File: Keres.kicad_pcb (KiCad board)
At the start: 6 copper layers, 110 x 70 mm, 168 parts, among them J1 XT90M, J2 DSUB44S_HD, J3 U_FL-R-SMT-1_10_, J4 2.54mm Pin Header, Q1 SiS443DN, Q2 SQJQ116EL, Q3 SQJQ116EL, Q4 SQJQ116EL, Q5 SQJQ116EL, U1 TLV76133DCY, U10 LT6106, U11 LT6106, U12 LT6106, U13 MAX11616, U14 LT6106, U15 LT6106, U16 LT6106, U17 LT6106, U18 MAX11614, U19 LT6106, U2 LM22678TJ-5, U3 LM22678TJ-5, U4 LM22678TJ-5, U5 BMP280, U6 MAX-M10S, U7 Teensy 4.0, U8 MPU-6050, U9 LT6106

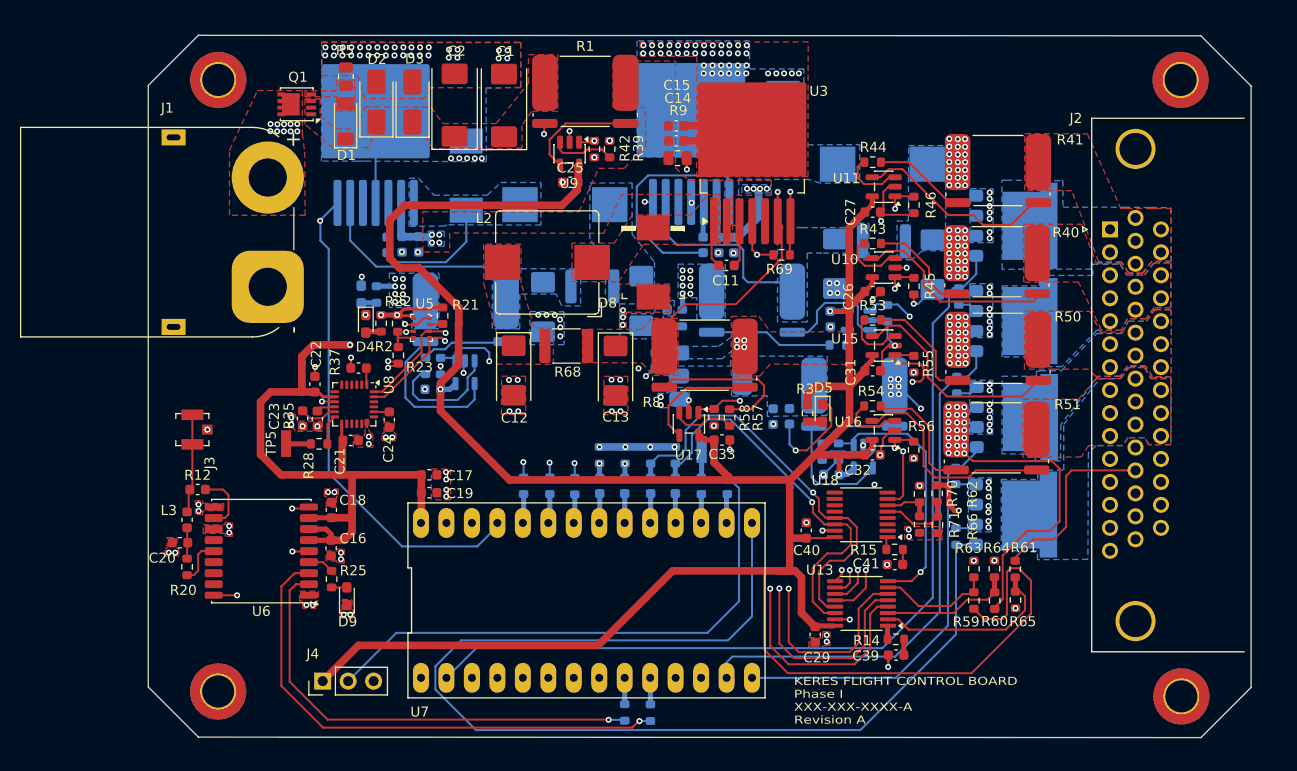
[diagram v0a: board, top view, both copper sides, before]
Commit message: Fix DRC Errors and Warnings
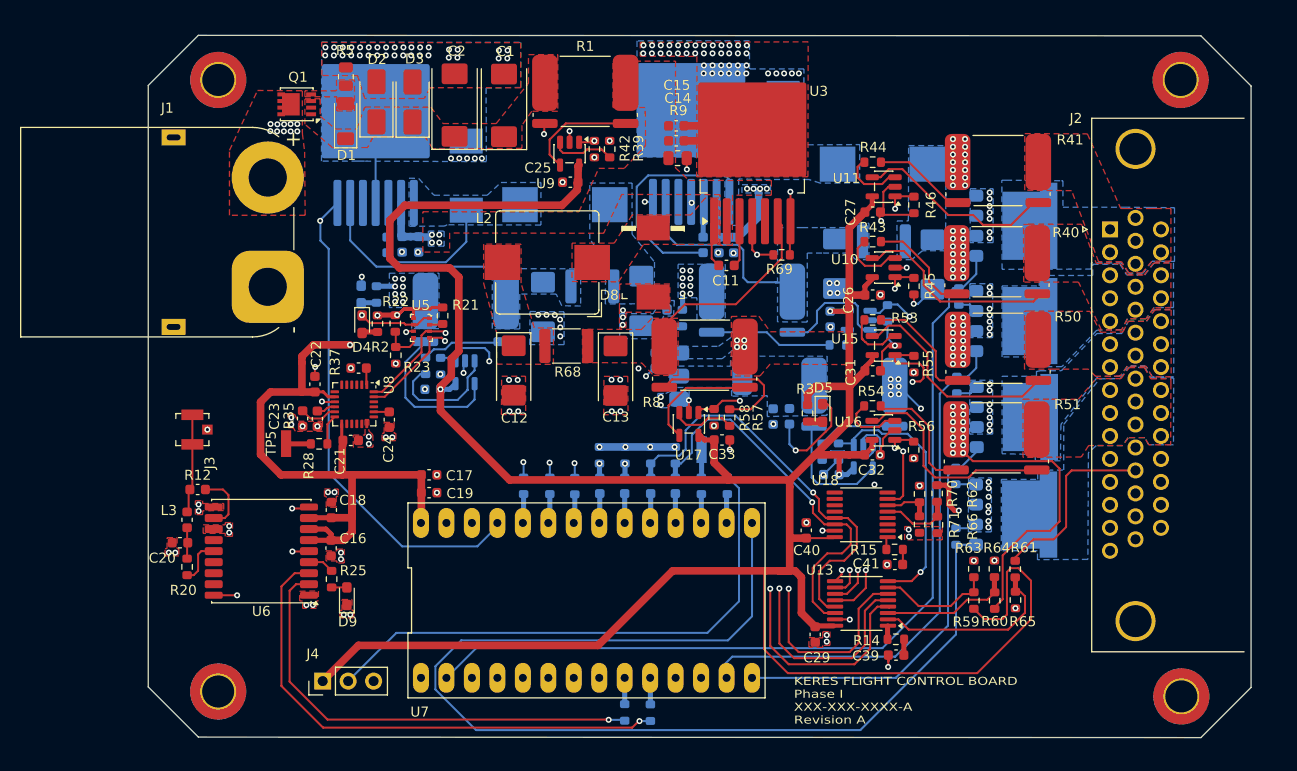
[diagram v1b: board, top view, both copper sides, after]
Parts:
- moved D4 0.37 mm to (56.4, 56.4)
- moved R2 0.37 mm to (57.9, 56.3)
- moved C26 0.35 mm to (107.3, 53.5)
- moved R23 0.25 mm to (59.7, 59.5)
- moved R22 0.25 mm to (59.7, 56.3)
- moved R43 0.18 mm to (107.3, 48.1)
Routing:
- net GND: track 97.0 -> 101.2 mm, vias 210 -> 205
- net /Power/5V0_FB: track 23.4 -> 20.5 mm, vias 1 -> 0
- net 5V0: track 281.5 -> 283.8 mm
- net 3V3: track 103.1 -> 104.1 mm, vias 18 -> 16
- net Net-(U5-SDO): track 3.24 -> 3.97 mm
- net VBUS_RAW: vias 94 -> 66
- net /IVSense/VBUS_MAIN_ISNS-: vias 4 -> 2
- removed copper zone on In2.Cu, net GND
- removed copper zone on In3.Cu, net GND

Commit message: Update PCBA Layout
Redo full PCBA layout
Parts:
- C11, C12, C13, C14, C15, D8, L2, R68, R69, R8, R9, U3: moved to B.Cu
- C28, C30, C4, C42, C5, C6, D11, D6, R11, R24, R26, R27, R29, R30, R32, R33, R36, R38, R4, R47, R48, R49, R52, R72, R73, R74, R75, R76, R77, TP6, U1, U12, U14, U19: moved to F.Cu
- R7: value CSS4J-4026R-1L00FE -> BVT-I-R005-1.0; footprint Resistor_SMD:R_Shunt_Isabellenhuette_BVR4026 -> Resistor_SMD:R_Shunt_Vishay_WSK2512_6332Metric_T1.19mm; moved to F.Cu
- moved R60 77.7 mm to (54.1, 42.0), turned to -90 degrees
- moved R64 74.5 mm to (54.1, 45.1), turned to -90 degrees
- moved D6 60.7 mm to (114.8, 37.2)
- moved R4 57.5 mm to (112.9, 37.3)
- moved R6 51.9 mm to (114.2, 34.1), turned to 0 degrees
- moved R59 50.9 mm to (108.9, 33.8)
- moved R65 50.4 mm to (114.8, 33.9)
- moved C41 50.1 mm to (80.3, 39.6), turned to 90 degrees
- moved C39 49.8 mm to (80.3, 49.1), turned to 90 degrees
- moved R15 48.0 mm to (81.9, 39.6), turned to -90 degrees
- moved R61 47.7 mm to (113.0, 33.9), turned to 90 degrees
- moved U3 47.7 mm to (59.1, 69.5), turned to 180 degrees
- moved R14 47.6 mm to (81.9, 49.1), turned to -90 degrees
- moved R63 47.5 mm to (110.7, 33.8), turned to -90 degrees
- moved C28 46.1 mm to (99.9, 34.6), turned to 180 degrees
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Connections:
- R72 pad 1: Net-(U19-+) -> Net-(U19--)
- R72 pad 2: /IVSense/5V0_SRVO2_ISNS+ -> /IVSense/5V0_SRVO2_ISNS-
- U13 pad 10: /IVSense/ESC2_ISNS -> /IVSense/5V0_ISNS
- U13 pad 11: /IVSense/ESC3_ISNS -> /IVSense/ESC2_ISNS
- U13 pad 12: /IVSense/ESC4_ISNS -> /IVSense/ESC1_ISNS
- U13 pad 2: /IVSense/5V0_SRVO1_VSNS -> /IVSense/5V0_VSNS
- U13 pad 4: /IVSense/5V0_SRVO1_ISNS -> unconnected-(U13-AIN8-Pad4)
- U13 pad 5: /IVSense/5V0_ISNS -> /IVSense/5V0_SRVO1_VSNS
- U13 pad 7: /IVSense/5V0_VSNS -> /IVSense/ESC4_ISNS
- U13 pad 9: /IVSense/ESC1_ISNS -> /IVSense/ESC3_ISNS
- U18 pad 11: unconnected-(U18-AIN6-Pad11) -> /IVSense/5V0_SRVO2_ISNS
- U18 pad 12: unconnected-(U18-AIN7-Pad12) -> /IVSense/5V0_SRVO1_ISNS
- U18 pad 7: /IVSense/5V0_SRVO2_ISNS -> unconnected-(U18-AIN2-Pad7)
- U19 pad 3: /IVSense/5V0_SRVO2_ISNS- -> Net-(U19--)
- U19 pad 4: Net-(U19-+) -> /IVSense/5V0_SRVO2_ISNS+
- U7 pad 13: /Microcontroller/ESC2_EN -> /Microcontroller/ESC3_EN
- U7 pad 14: /Microcontroller/ESC3_EN -> /Microcontroller/ESC4_EN
- U7 pad 15: /Microcontroller/ESC4_EN -> /Microcontroller/ESC1_EN
- U7 pad 2: /Microcontroller/ESC1_EN -> /Microcontroller/ESC2_EN
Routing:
- net 5V0: track 283.8 -> 24.0 mm, vias 7 -> 23
- net /Microcontroller/ESC4_EN: track 113.8 -> 32.0 mm
- net /IVSense/5V0_SRVO1_ISNS: track 75.8 -> 12.7 mm, vias 2 -> 0
- net /IVSense/VBUS_MAIN_ISNS: track 75.1 -> 27.4 mm, vias 2 -> 0
- net Net-(U6-~{SAFEBOOT}): track 48.9 -> 2.33 mm, vias 2 -> 0
- net /Microcontroller/nSAFEBOOT: track 2.94 -> 47.1 mm, vias 0 -> 1
- net /Microcontroller/ESC1_EN: track 88.3 -> 44.1 mm
- net /IVSense/5V0_SRVO2_VSNS: track 4.71 -> 45.0 mm, vias 0 -> 2
- net Net-(U6-EXTINT): track 41.9 -> 3.48 mm, vias 2 -> 0
- net Net-(U6-~{RESET}): track 36.1 -> 2.27 mm, vias 2 -> 0
- net /IVSense/5V0_ISNS: track 46.3 -> 14.4 mm, vias 2 -> 0
- net /RCVR_PPM: track 55.2 -> 87.0 mm, vias 0 -> 1
- net Net-(U4-FB): track 20.6 -> 50.6 mm
- net Net-(U2-FB): track 22.9 -> 52.4 mm
- net /Microcontroller/nRESET: track 2.90 -> 31.0 mm, vias 0 -> 1
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- added copper zone on B.Cu, net /Power/5V0_FB
- added copper zone on In3.Cu, net 5V0
- added copper zone on In3.Cu, net 5V0_SRVO_BUS1
- added copper zone on In3.Cu, net 5V0_SRVO_BUS2
- added copper zone on In2.Cu, net GND
- added copper zone on In3.Cu, net GND
- added copper zone on B.Cu, net Net-(C12-Pad1)
- added copper zone on F.Cu, net Net-(U1-VO)
- added copper zone on B.Cu, net Net-(U3-SW)
- added copper zone on In1.Cu, net VBUS_ESC1
- added copper zone on In1.Cu, net VBUS_ESC2
- added copper zone on In1.Cu, net VBUS_ESC3
- added copper zone on In1.Cu, net VBUS_ESC4
- added copper zone on In3.Cu, net VBUS_MAIN
- removed copper zone on F.Cu, net /Power/5V0_FB
- removed copper zone on In1.Cu, net 3V3
- removed copper zone on B.Cu, net 5V0
- removed copper zone on B.Cu, net 5V0_SRVO_BUS1
- removed copper zone on In2.Cu, net 5V0_SRVO_BUS1
- removed copper zone on B.Cu, net 5V0_SRVO_BUS2
- removed copper zone on In2.Cu, net 5V0_SRVO_BUS2
- removed copper zone on In4.Cu, net ESC1_RTN
- removed copper zone on In4.Cu, net ESC2_RTN
- removed copper zone on In4.Cu, net ESC3_RTN
- removed copper zone on In4.Cu, net ESC4_RTN
- removed copper zone on F.Cu, net Net-(C12-Pad1)
- removed copper zone on B.Cu, net Net-(U1-VO)
- removed copper zone on F.Cu, net Net-(U3-SW)
- removed copper zone on In2.Cu, net VBUS_ESC1
- removed copper zone on In2.Cu, net VBUS_ESC2
- removed copper zone on In2.Cu, net VBUS_ESC3
- removed copper zone on In2.Cu, net VBUS_ESC4
- removed copper zone on F.Cu, net VBUS_MAIN
- removed copper zone on In2.Cu, net VBUS_RAW
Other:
- rule pad_to_mask_clearance: 0.1 -> 0.1016
- rule solder_mask_min_width: 0.1 -> 0.1016

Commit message: Update BOM, Gerber Outputs, Fiducials
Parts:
- added FID1: Fiducial, Fiducial:Fiducial_0.75mm_Mask1.5mm, F.Cu at (133.8, 32.5)
- added FID2: Fiducial, Fiducial:Fiducial_0.75mm_Mask1.5mm, F.Cu at (48.5, 31.9)
- added FID3: Fiducial, Fiducial:Fiducial_0.75mm_Mask1.5mm, F.Cu at (48.5, 91.0)
- added FID4: Fiducial, Fiducial:Fiducial_0.75mm_Mask1.5mm, B.Cu at (48.5, 31.9)
- added FID5: Fiducial, Fiducial:Fiducial_0.75mm_Mask1.5mm, B.Cu at (48.5, 91.0)
- added FID6: Fiducial, Fiducial:Fiducial_0.75mm_Mask1.5mm, B.Cu at (133.8, 31.9)
- R42, R45, R46, R48, R52, R55, R56, R58, R63, R73: value 8K -> 8.06K
- R60: value 8K -> 10K
- R61, R62, R70: value 2K -> 10K
- R64: value 1K -> 1.6K
- R65, R71: value 8K -> 18K
- R66: value 6K -> 150K
